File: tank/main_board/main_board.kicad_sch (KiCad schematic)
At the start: 39 parts, among them J1 Encoder0, J11 M0, J12 M1, J13 M2, J14 Spk, J15 LEDs, J16 SigOut, J2 Encoder1, J3 Encoder2, J4 Encoder3, J5 Programming Header, J6 Bump0, J7 Bump1, J8 PowerOut, J9 PowerIn, U1 L7805, U2 ATMEGA328P-PU, U3 SN74HC595, U4 L293D, U5 L293D, Y1 Crystal

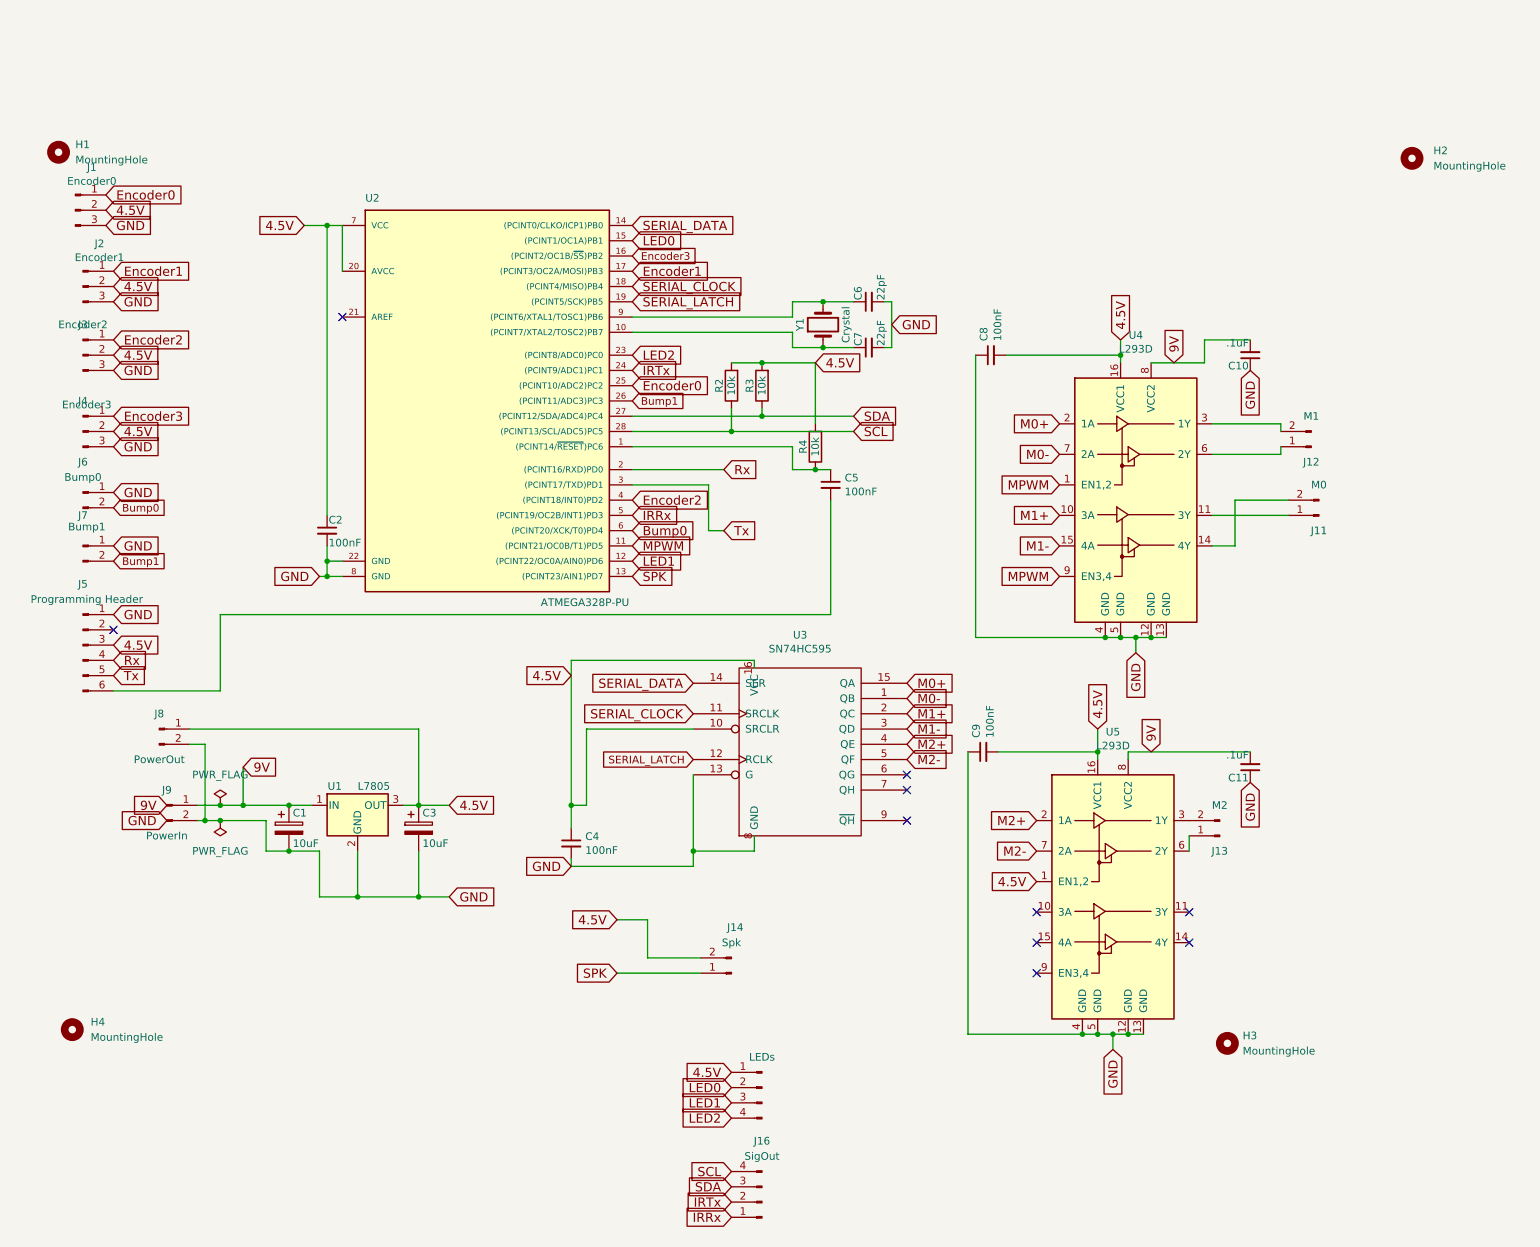
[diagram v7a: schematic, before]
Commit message: Main Board v0.18 Attempting to prevent uC reset due to motor noise and/or brownout - added TVS diode - added more capacitors
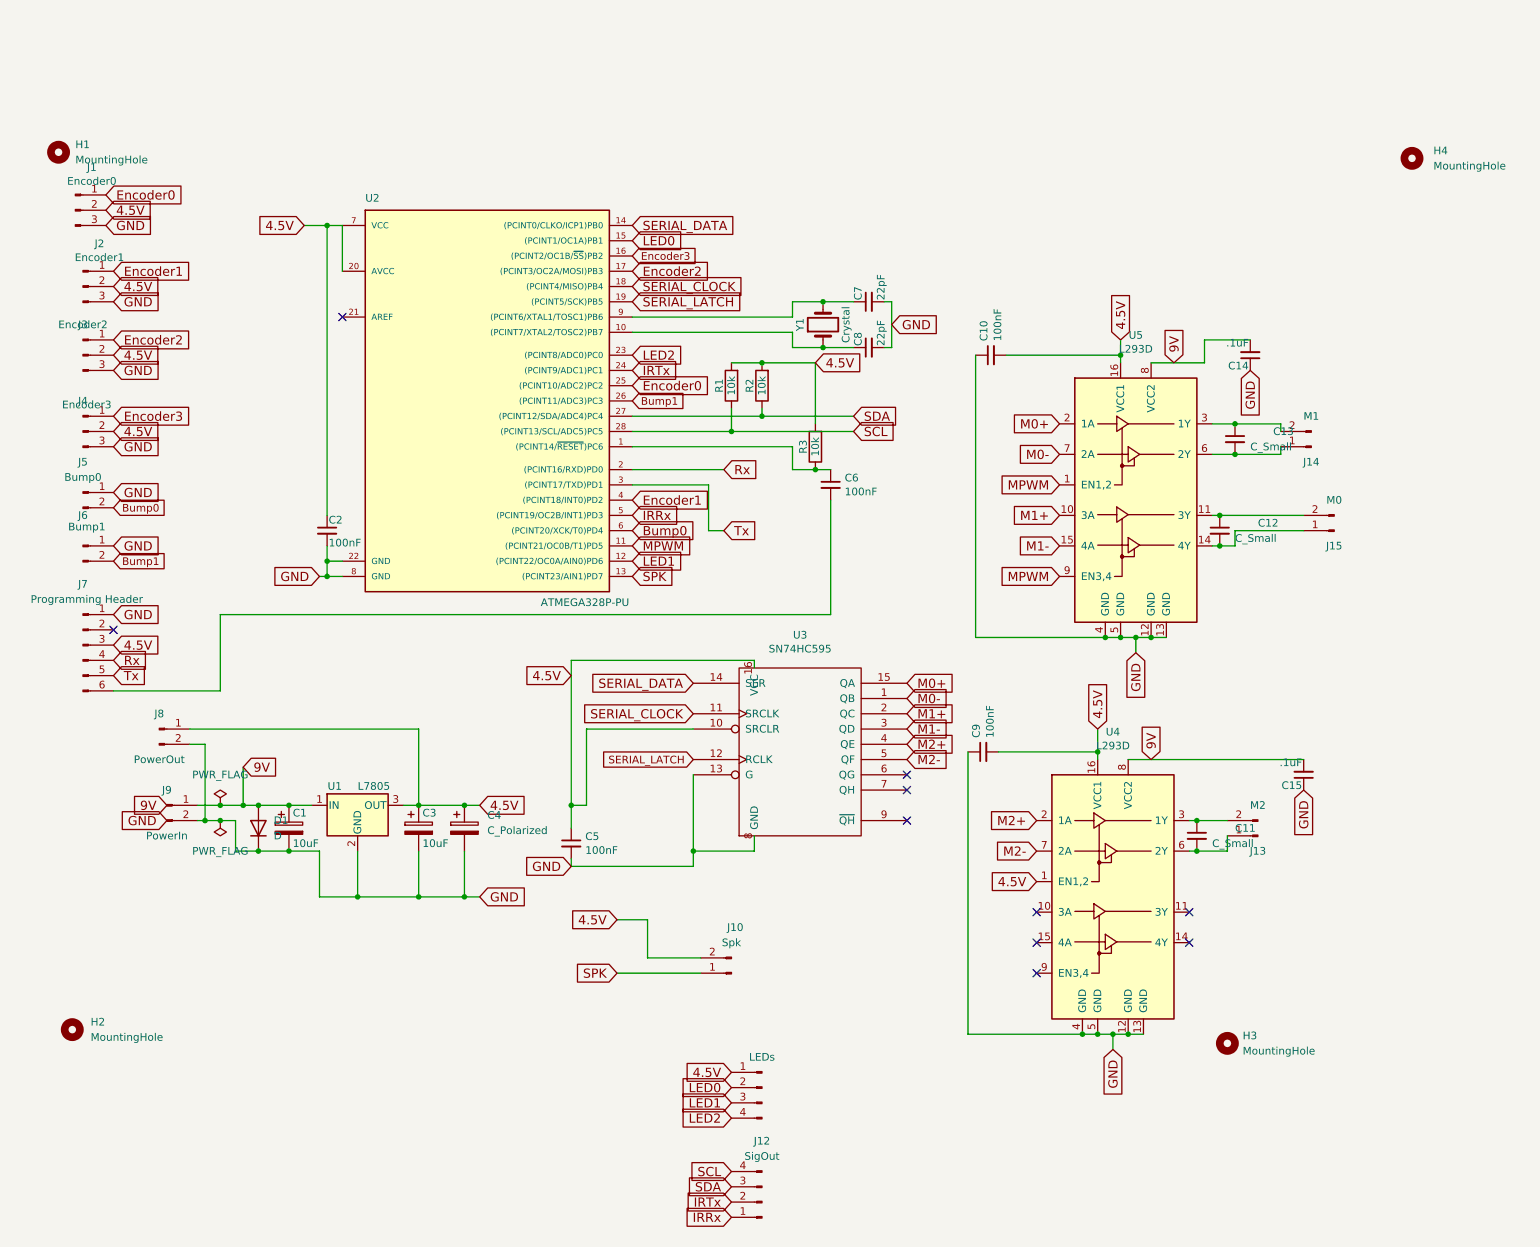
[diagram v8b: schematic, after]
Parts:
- added C11, C12, C13: C_Small, Capacitor_THT:C_Disc_D5.0mm_W2.5mm_P2.50mm, symbol Device:C_Small
- added C4: C_Polarized, Capacitor_THT:CP_Radial_D6.3mm_P2.50mm, symbol Device:C_Polarized
- added D1: D, Diode_THT:D_DO-15_P10.16mm_Horizontal, symbol Device:D
- renumbered C8 to C10, C10 to C14, C11 to C15, C4 to C5, C5 to C6, C6 to C7, C7 to C8, H4 to H2, H2 to H4, J14 to J10, J15 to J11, J16 to J12, J12 to J14, J11 to J15, J6 to J5, J7 to J6, J5 to J7, R2 to R1, R3 to R2, R4 to R3, U5 to U4, U4 to U5
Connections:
- net 4.5V: now also C4.1
- net 9V: now also D1.2 (A)
- net Encoder1: now also U2.4 ((PCINT18/INT0)PD2); no longer U2.17 ((PCINT3/OC2A/MOSI)PB3)
- net Encoder2: now also U2.17 ((PCINT3/OC2A/MOSI)PB3); no longer U2.4 ((PCINT18/INT0)PD2)
- net GND: now also C4.2, D1.1 (K)
- net at J13.2 (Pin_2), U4.3 (1Y): now also C11.1
- net at J13.1 (Pin_1), U4.6 (2Y): now also C11.2
- net at J14.1 (Pin_1), U5.6 (2Y): now also C13.2
- net at J14.2 (Pin_2), U5.3 (1Y): now also C13.1
- net at J15.1 (Pin_1): now also U5.14 (4Y), C12.2; no longer U5.11 (3Y)
- net at J15.2 (Pin_2): now also U5.11 (3Y), C12.1; no longer U5.14 (4Y)
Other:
- moved on the sheet: C15, J13, J15
